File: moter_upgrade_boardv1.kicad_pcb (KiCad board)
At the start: 2 copper layers, 1 part

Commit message: 電源供給を切り替えられるように変更 部品配置の変更
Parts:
- added C1: 4.7μF, Capacitor_SMD:C_0805_2012Metric_Pad1.18x1.45mm_HandSolder, B.Cu at (75.8, 56.2)
- added C10: 0.1uF, Capacitor_SMD:C_0603_1608Metric_Pad1.08x0.95mm_HandSolder, B.Cu at (58.7, 67.4)
- added C11: 0.1uf, Capacitor_SMD:C_0603_1608Metric_Pad1.08x0.95mm_HandSolder, B.Cu at (55.8, 76.5)
- added C12: 1uf, Capacitor_SMD:C_0603_1608Metric_Pad1.08x0.95mm_HandSolder, B.Cu at (54.3, 76.5)
- added C13: 0.1uf, Capacitor_SMD:C_0603_1608Metric_Pad1.08x0.95mm_HandSolder, B.Cu at (74.7, 73.7)
- added C14: 1uf, Capacitor_SMD:C_0603_1608Metric_Pad1.08x0.95mm_HandSolder, B.Cu at (59.3, 82.2)
- added C15: 4.7μF, Capacitor_SMD:C_0805_2012Metric_Pad1.18x1.45mm_HandSolder, B.Cu at (74.2, 87.4)
- added C16: 4.7μF, Capacitor_SMD:C_0805_2012Metric_Pad1.18x1.45mm_HandSolder, B.Cu at (74.2, 82.9)
- added C17: 22μF, Capacitor_SMD:C_0805_2012Metric_Pad1.18x1.45mm_HandSolder, B.Cu at (74.2, 80.9)
- added C2: 4.7μF, Capacitor_SMD:C_0805_2012Metric_Pad1.18x1.45mm_HandSolder, B.Cu at (75.7, 60.8)
- added C3: 22μF, Capacitor_SMD:C_0805_2012Metric_Pad1.18x1.45mm_HandSolder, B.Cu at (75.7, 62.8)
- added C4: 2.2μF, Capacitor_SMD:C_0603_1608Metric_Pad1.08x0.95mm_HandSolder, B.Cu at (62.9, 76.2)
- added C5: 2.2μF, Capacitor_SMD:C_0603_1608Metric_Pad1.08x0.95mm_HandSolder, B.Cu at (60.2, 67.4)
- added C6: 0.1uF, Capacitor_SMD:C_0603_1608Metric_Pad1.08x0.95mm_HandSolder, B.Cu at (56.4, 71.4)
- added C7: 0.1uF, Capacitor_SMD:C_0603_1608Metric_Pad1.08x0.95mm_HandSolder, B.Cu at (64.4, 76.2)
- added C8: 0.1uF, Capacitor_SMD:C_0603_1608Metric_Pad1.08x0.95mm_HandSolder, B.Cu at (67.0, 71.2)
- added C9: 4.7uf, Capacitor_SMD:C_0805_2012Metric_Pad1.18x1.45mm_HandSolder, B.Cu at (67.2, 69.4)
- added D1: D_Shockley, Diode_SMD:D_SOD-323_HandSoldering, B.Cu at (76.0, 58.5)
- added D2: LED_GREEN, Capacitor_SMD:C_0603_1608Metric_Pad1.08x0.95mm_HandSolder, B.Cu at (79.4, 86.4)
- added D3: D_Shockley, Diode_SMD:D_SOD-323_HandSoldering, B.Cu at (74.3, 85.5)
- added D4: LED_RED, Capacitor_SMD:C_0603_1608Metric_Pad1.08x0.95mm_HandSolder, F.Cu at (79.4, 82.4)
- added H1: MountingHole, MountingHole:MountingHole_3.2mm_M3, F.Cu at (54.0, 54.0)
- added H2: MountingHole, MountingHole:MountingHole_3.2mm_M3, F.Cu at (89.0, 54.0)
- added H3: MountingHole, MountingHole:MountingHole_3.2mm_M3, F.Cu at (54.0, 103.8)
- added H4: MountingHole, MountingHole:MountingHole_3.2mm_M3, F.Cu at (89.0, 103.8)
- added J1: Conn_01x04_Socket, Connector_PinHeader_2.54mm:PinHeader_1x04_P2.54mm_Vertical, F.Cu at (70.3, 66.9)
- added J2: Conn_01x03_Socket, Connector_PinHeader_2.54mm:PinHeader_1x03_P2.54mm_Vertical, F.Cu at (79.5, 104.5)
- added J3: Conn_01x02_Socket, Connector_AMASS:AMASS_XT30PW-M_1x02_P2.50mm_Horizontal, F.Cu at (68.2, 61.5)
- added J4: Conn_01x02_Socket, Connector_JST:JST_XH_S2B-XH-A-1_1x02_P2.50mm_Horizontal, F.Cu at (89.3, 66.1)
- added J5: Conn_01x02_Socket, Connector_JST:JST_XH_S2B-XH-A-1_1x02_P2.50mm_Horizontal, F.Cu at (53.9, 63.4)
- added J6: Conn_01x02_Socket, Connector_AMASS:AMASS_XT30PW-M_1x02_P2.50mm_Horizontal, F.Cu at (62.2, 96.2)
- added J8: Conn_01x05_Socket, Connector_JST:JST_XH_S5B-XH-A-1_1x05_P2.50mm_Horizontal, F.Cu at (87.4, 84.0)
- added J9: USB_C_Receptacle_USB2.0_16P, Connector_USB:USB_C_Receptacle_GCT_USB4105-xx-A_16P_TopMnt_Horizontal, F.Cu at (53.7, 85.3)
- added JP1: Jumper_3_Bridged12, Connector_PinSocket_2.54mm:PinSocket_1x03_P2.54mm_Vertical, F.Cu at (60.8, 91.5)
- added R1: 68, Resistor_SMD:R_0603_1608Metric_Pad0.98x0.95mm_HandSolder, B.Cu at (80.7, 97.1)
- added R10: 5.1k, Resistor_SMD:R_0603_1608Metric_Pad0.98x0.95mm_HandSolder, B.Cu at (54.4, 84.0)
- added R2: 68, Resistor_SMD:R_0603_1608Metric_Pad0.98x0.95mm_HandSolder, B.Cu at (74.7, 95.6)
- added R3: 1k, Resistor_SMD:R_0603_1608Metric_Pad0.98x0.95mm_HandSolder, B.Cu at (80.7, 95.6)
- added R4: 1k, Resistor_SMD:R_0603_1608Metric_Pad0.98x0.95mm_HandSolder, B.Cu at (74.7, 97.1)
- added R5: 10K, Resistor_SMD:R_0603_1608Metric_Pad0.98x0.95mm_HandSolder, B.Cu at (60.4, 73.5)
- added R6: 120, Resistor_SMD:R_0603_1608Metric_Pad0.98x0.95mm_HandSolder, B.Cu at (81.6, 65.0)
- added R7: 1k, Resistor_SMD:R_0603_1608Metric_Pad0.98x0.95mm_HandSolder, F.Cu at (79.4, 86.4)
- added R8: 1k, Resistor_SMD:R_0603_1608Metric_Pad0.98x0.95mm_HandSolder, B.Cu at (79.4, 82.4)
- added R9: 5.1k, Resistor_SMD:R_0603_1608Metric_Pad0.98x0.95mm_HandSolder, B.Cu at (54.5, 87.1)
- added SW1: SW_SPDT, Button_Switch_THT:SW_Slide-03_Wuerth-WS-SLTV_10x2.5x6.4_P2.54mm, F.Cu at (51.5, 74.6)
- added SW2: SW_Push, Button_Switch_THT:SW_PUSH_6mm, F.Cu at (56.0, 92.2)
- added SW3: SW_Wuerth_450301014042, Button_Switch_THT:SW_Slide-03_Wuerth-WS-SLTV_10x2.5x6.4_P2.54mm, F.Cu at (77.7, 66.7)
- added U1: BD33FC0FP, Package_TO_SOT_SMD:TO-252-2, F.Cu at (79.4, 58.4)
- added U2: TLP785, Package_DIP:DIP-4_W7.62mm, F.Cu at (82.0, 94.1)
- added U3: TLP785, Package_DIP:DIP-4_W7.62mm, F.Cu at (76.0, 94.1)
- added U4: STM32H523CCTx, Package_QFP:LQFP-48_7x7mm_P0.5mm, F.Cu at (61.7, 74.2)
- added U5: MCP2562-E-P, Package_DIP:DIP-8_W7.62mm, F.Cu at (73.2, 69.8)
- added U6: CH340E, Package_SO:MSOP-10_3x3mm_P0.5mm, F.Cu at (60.6, 83.1)
- added U7: BD33FC0FP, Package_TO_SOT_SMD:TO-252-2, F.Cu at (67.7, 85.3)
- moved G*** 53.9 mm to (125.0, 61.0)
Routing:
- net GND1: track 0.00 -> 98.8 mm, vias 0 -> 5
- net +3.3V: track 0.00 -> 77.7 mm, vias 0 -> 8
- net +3V3: track 0.00 -> 73.5 mm, vias 0 -> 1
- net CAN_L: track 0.00 -> 47.1 mm
- net CAN_H: track 0.00 -> 44.3 mm
- net nrst: track 0.00 -> 41.4 mm, vias 0 -> 1
- net GND: track 0.00 -> 36.5 mm, vias 0 -> 9
- net +5V: track 0.00 -> 33.0 mm, vias 0 -> 3
- net dir to moter: track 0.00 -> 32.7 mm, vias 0 -> 1
- net Net-(D2-A): track 0.00 -> 27.5 mm, vias 0 -> 3
- net wm to moter: track 0.00 -> 25.6 mm, vias 0 -> 3
- net en-x: track 0.00 -> 25.0 mm
- net en-b: track 0.00 -> 24.7 mm
- net en-a: track 0.00 -> 24.1 mm
- net +24V: track 0.00 -> 16.0 mm, vias 0 -> 1
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- added copper zone on B.Cu, net GND
- added copper zone on F.Cu, net GND
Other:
- board outline added: 43 x 58 mm

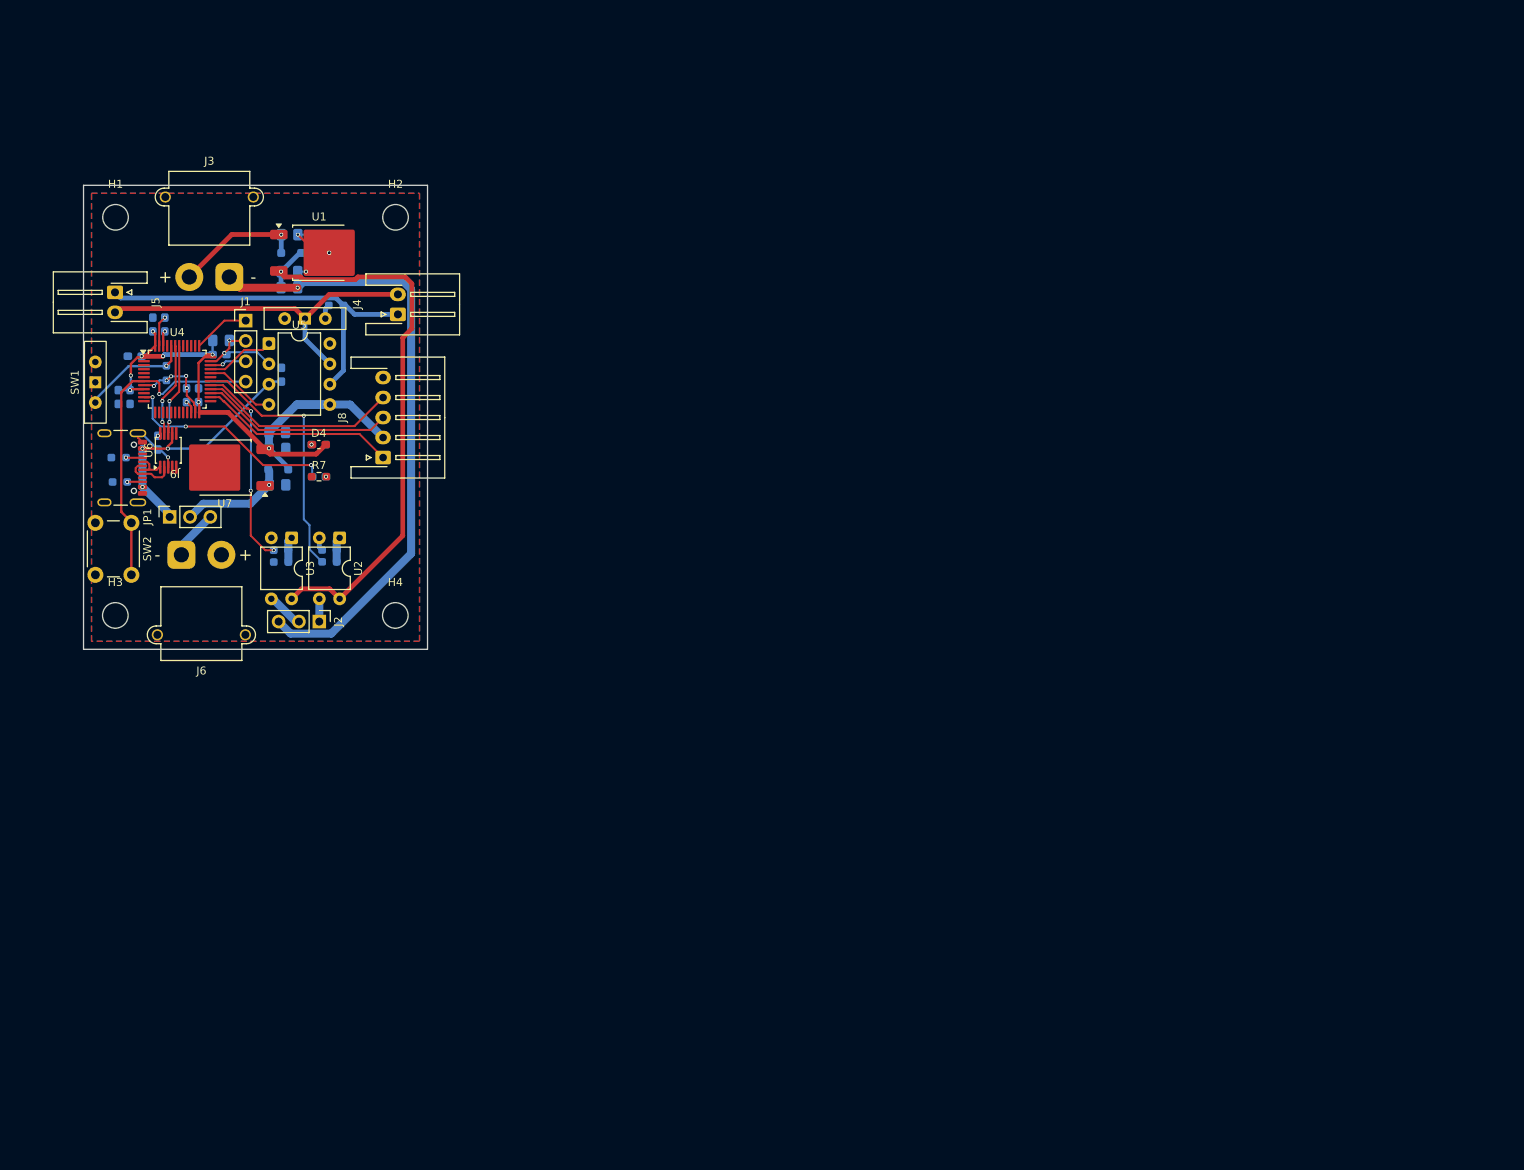
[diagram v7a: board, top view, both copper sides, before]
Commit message: stlinkをstdc14に対応させた　部品配置の変更
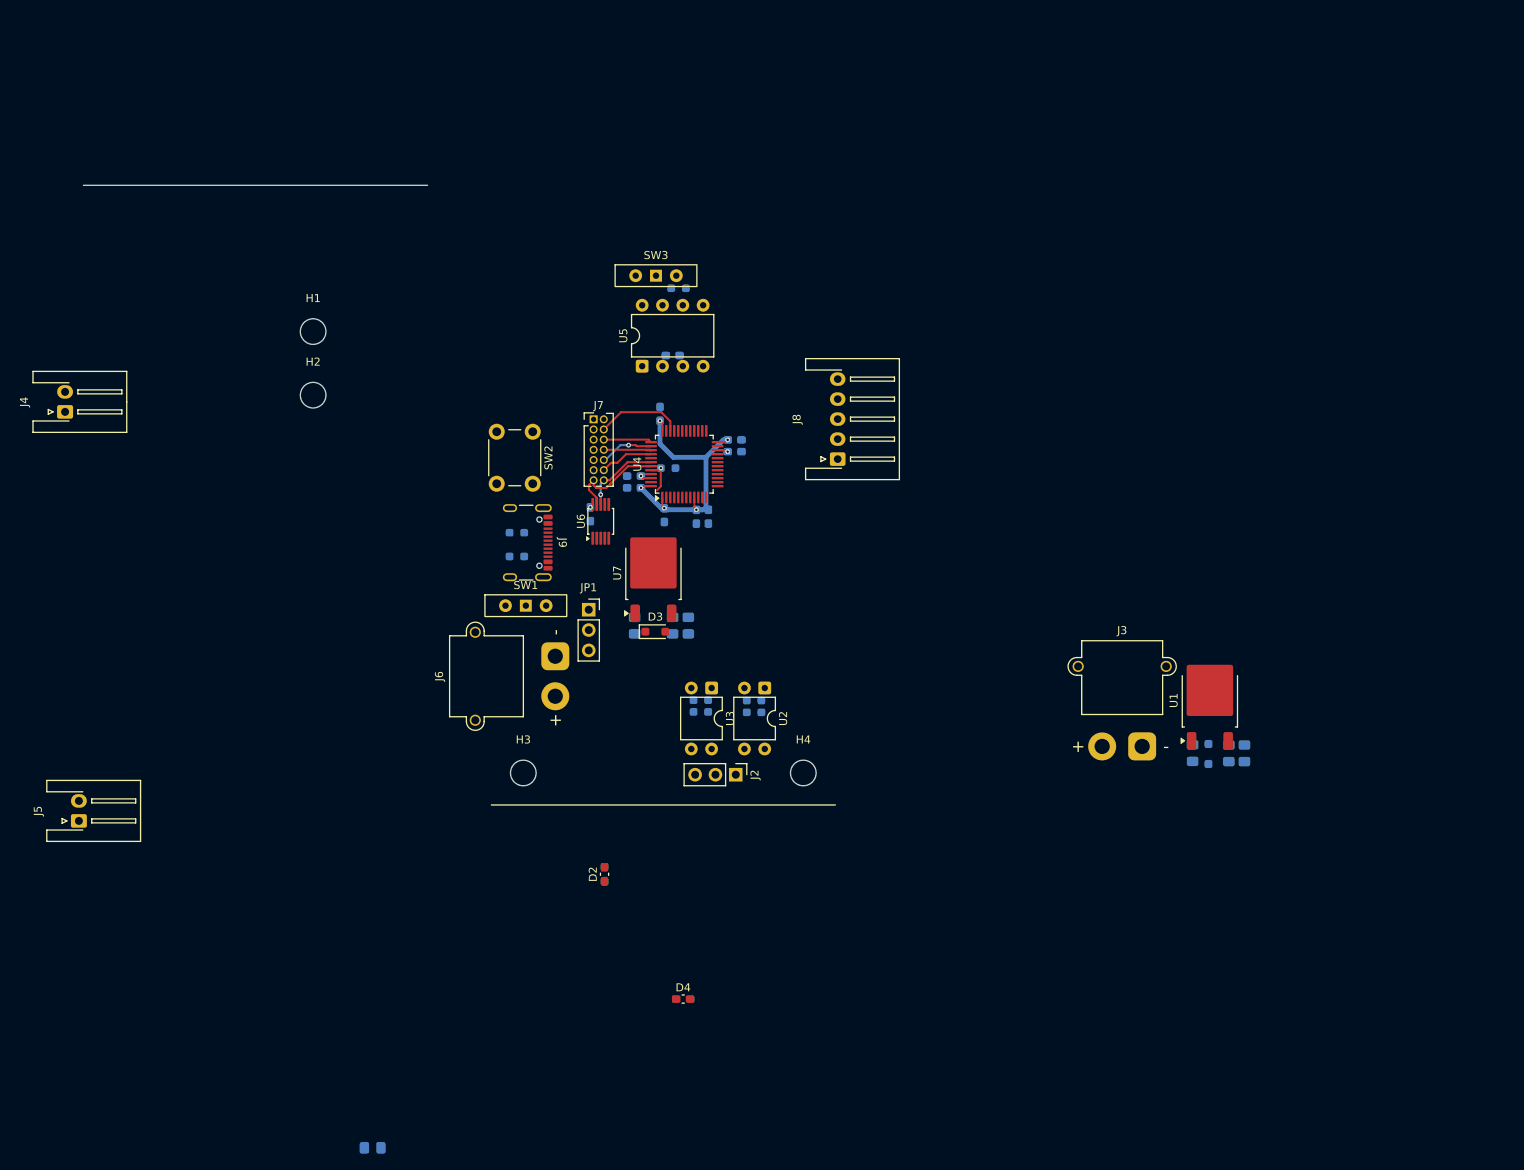
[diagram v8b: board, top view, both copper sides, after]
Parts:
- removed J1: Conn_01x04_Socket, Connector_PinHeader_2.54mm:PinHeader_1x04_P2.54mm_Vertical
- added J7: Conn_ST_STDC14, Connector_PinHeader_1.27mm:PinHeader_2x07_P1.27mm_Vertical, F.Cu at (113.8, 79.3)
- D2, D3: moved to F.Cu
- R7: moved to B.Cu
- moved C3 132.8 mm to (195.1, 121.0), turned to -90 degrees
- moved C2 132.0 mm to (193.2, 121.0), turned to -90 degrees
- moved D1 130.6 mm to (190.6, 121.1), turned to -90 degrees
- moved C1 130.2 mm to (188.6, 121.0), turned to -90 degrees
- moved J3 128.3 mm to (182.3, 120.1)
- moved U1 124.6 mm to (190.8, 114.4), turned to 90 degrees
- moved C9 102.7 mm to (86.1, 170.3), turned to 180 degrees
- moved G*** 93.8 mm to (39.0, 98.5)
- moved R8 82.9 mm to (125.0, 151.7)
- moved D4 82.9 mm to (125.0, 151.7)
- moved C12 75.3 mm to (128.1, 91.4)
- moved C11 72.4 mm to (126.6, 91.4)
- moved C6 69.1 mm to (122.6, 91.2), turned to -90 degrees
- moved C4 68.9 mm to (131.4, 83.3), turned to 180 degrees
- moved C7 67.2 mm to (131.4, 81.8), turned to 0 degrees
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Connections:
- U4 pad 38: unconnected-(U4-PA15(JTDI)-Pad38) -> jtdi
- U4 pad 39: unconnected-(U4-PB3(JTDO-Pad39) -> swo
- U4 pad 40: unconnected-(U4-PB4(NJTRST)-Pad40) -> trst
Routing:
- net GND1: track 98.8 -> 0.00 mm, vias 5 -> 0
- net +3V3: track 73.5 -> 0.00 mm, vias 1 -> 0
- net CAN_L: track 47.1 -> 0.00 mm
- net CAN_H: track 44.3 -> 0.00 mm
- net nrst: track 41.4 -> 0.00 mm, vias 1 -> 0
- net +3.3V: track 77.7 -> 37.7 mm, vias 8 -> 5
- net GND: track 36.5 -> 0.00 mm, vias 9 -> 0
- net +5V: track 33.0 -> 0.00 mm, vias 3 -> 0
- net dir to moter: track 32.7 -> 0.00 mm, vias 1 -> 0
- net Net-(D2-A): track 27.5 -> 0.00 mm, vias 3 -> 0
- net wm to moter: track 25.6 -> 0.00 mm, vias 3 -> 0
- net en-x: track 25.0 -> 0.00 mm
- net en-b: track 24.7 -> 0.00 mm
- net en-a: track 24.1 -> 0.00 mm
- net +24V: track 16.0 -> 0.00 mm, vias 1 -> 0
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- removed copper zone on B.Cu, net GND
- removed copper zone on F.Cu, net GND
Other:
- board outline removed
